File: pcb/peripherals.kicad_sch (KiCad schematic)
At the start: 10 parts, among them J1 Micro_SD_Card, J10 I2C3, J6 I2C1, J9 I2C2, U9 OLED128X64

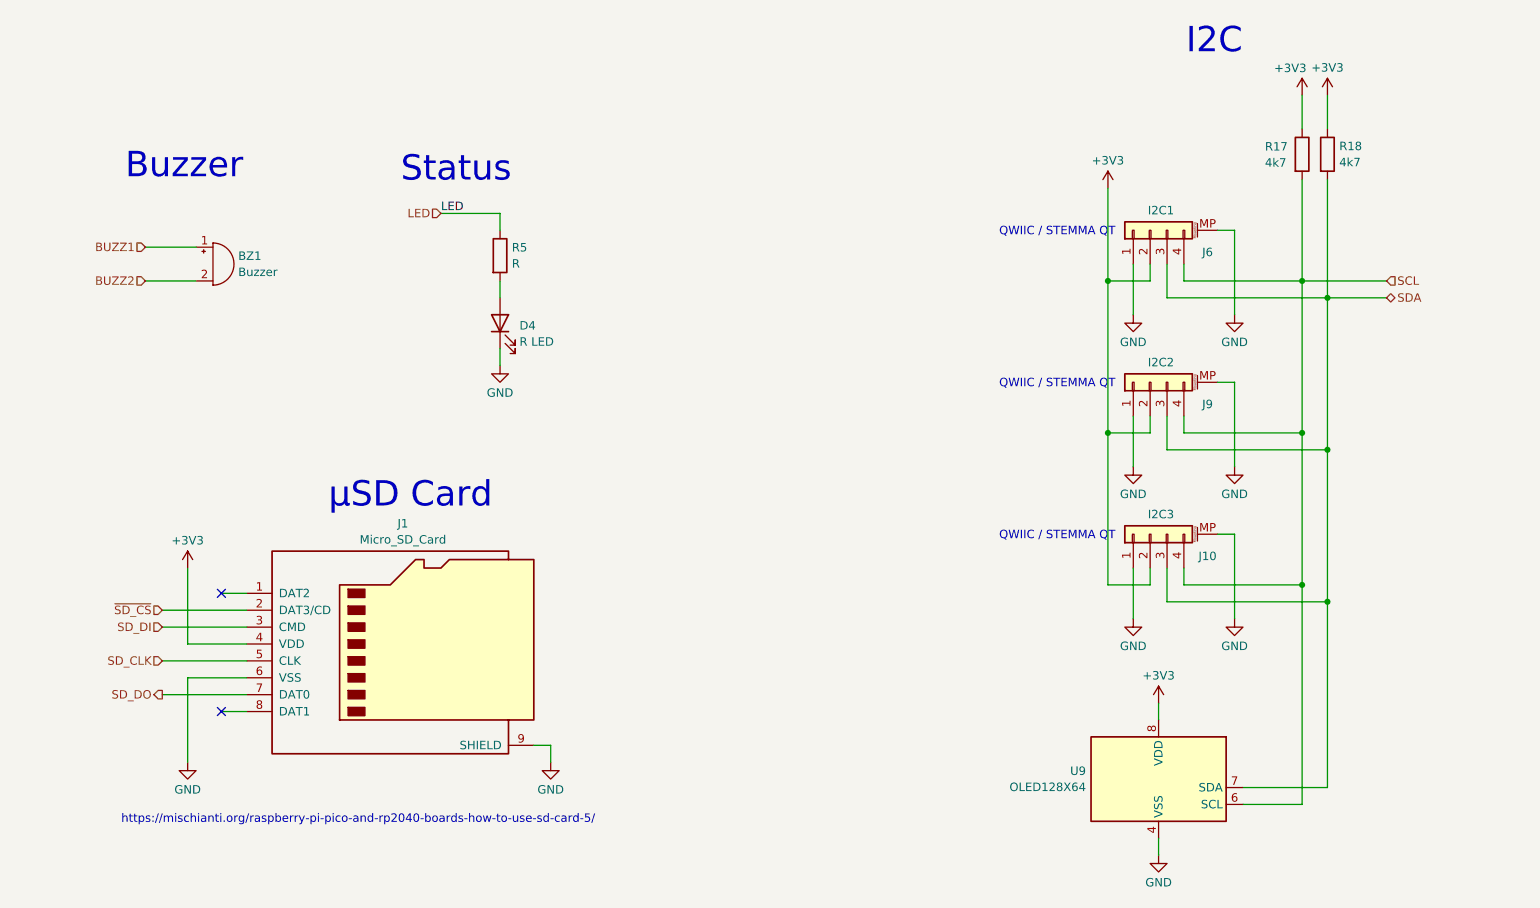
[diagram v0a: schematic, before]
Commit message: Added some transient protection
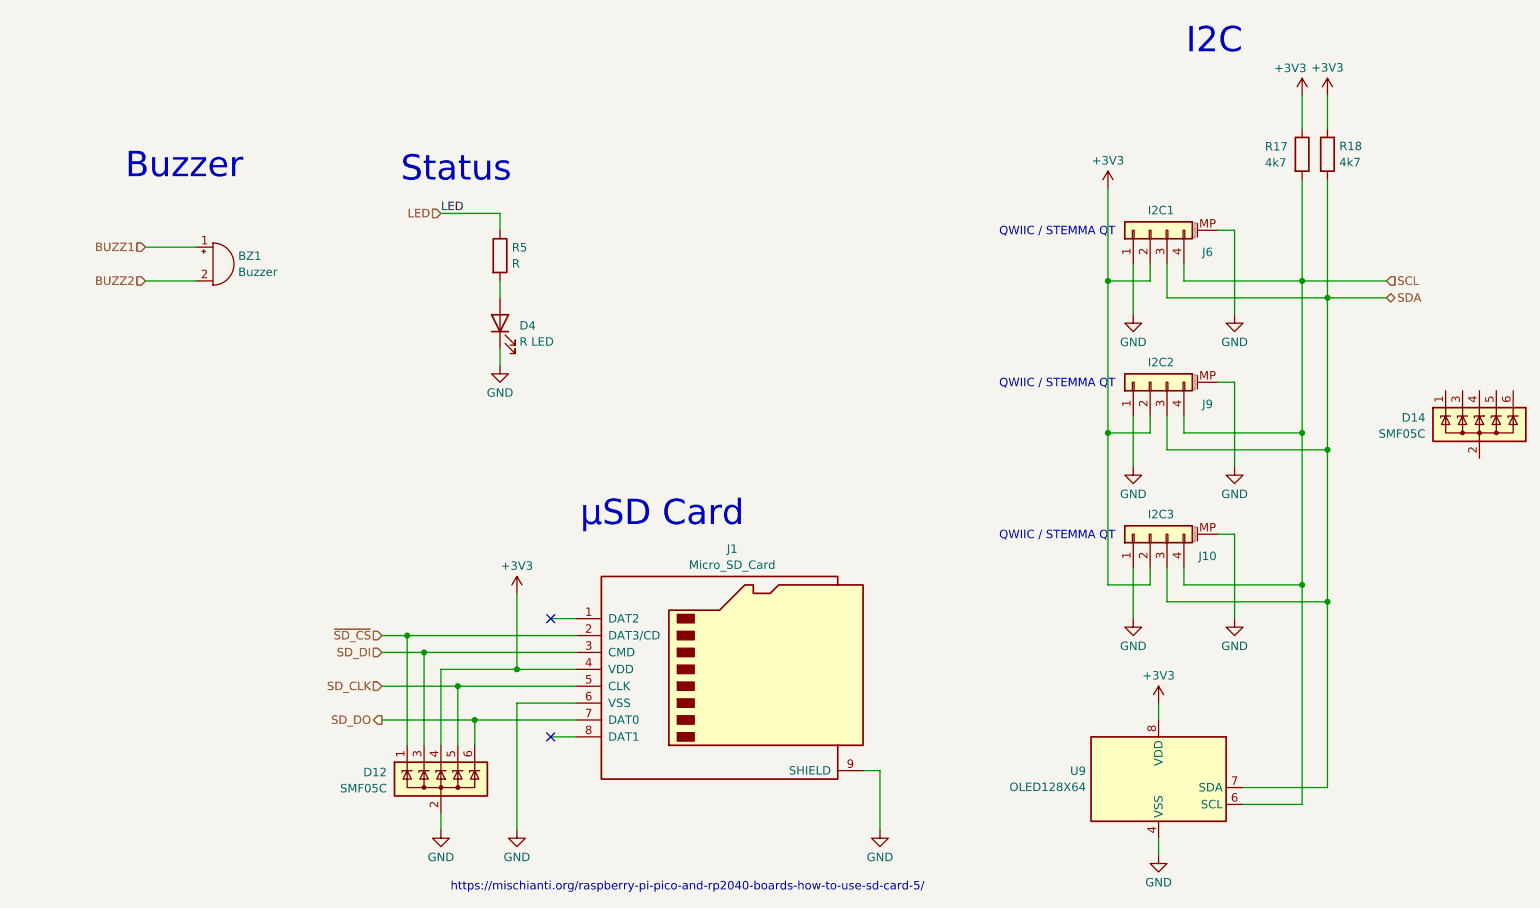
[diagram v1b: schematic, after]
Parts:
- added D12, D14: SMF05C, Package_TO_SOT_SMD:SOT-363_SC-70-6_Handsoldering, symbol Power_Protection:SP0505BAHT
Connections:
- net +3V3: now also D12.4 (K)
- net GND: now also D12.2 (A)
- net SD_CLK: now also D12.5 (K)
- net SD_DI: now also D12.3 (K)
- net SD_DO: now also D12.6 (K)
- net ~{SD_CS}: now also D12.1 (K)
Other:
- moved on the sheet: J1
